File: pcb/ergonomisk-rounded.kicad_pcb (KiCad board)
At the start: 4 copper layers, 135.5 x 109 mm, 63 parts

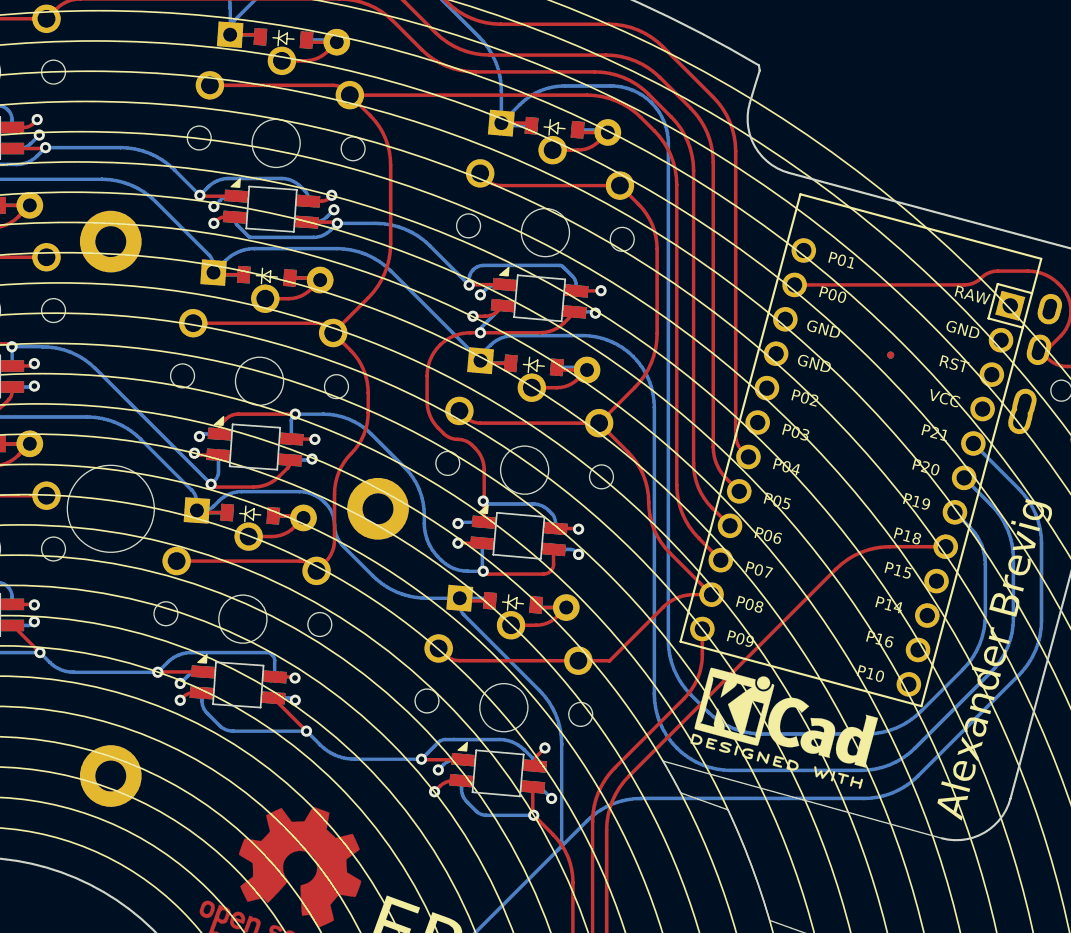
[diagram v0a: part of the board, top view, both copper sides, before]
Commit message: fix: JCL found an issue and I should've found it too
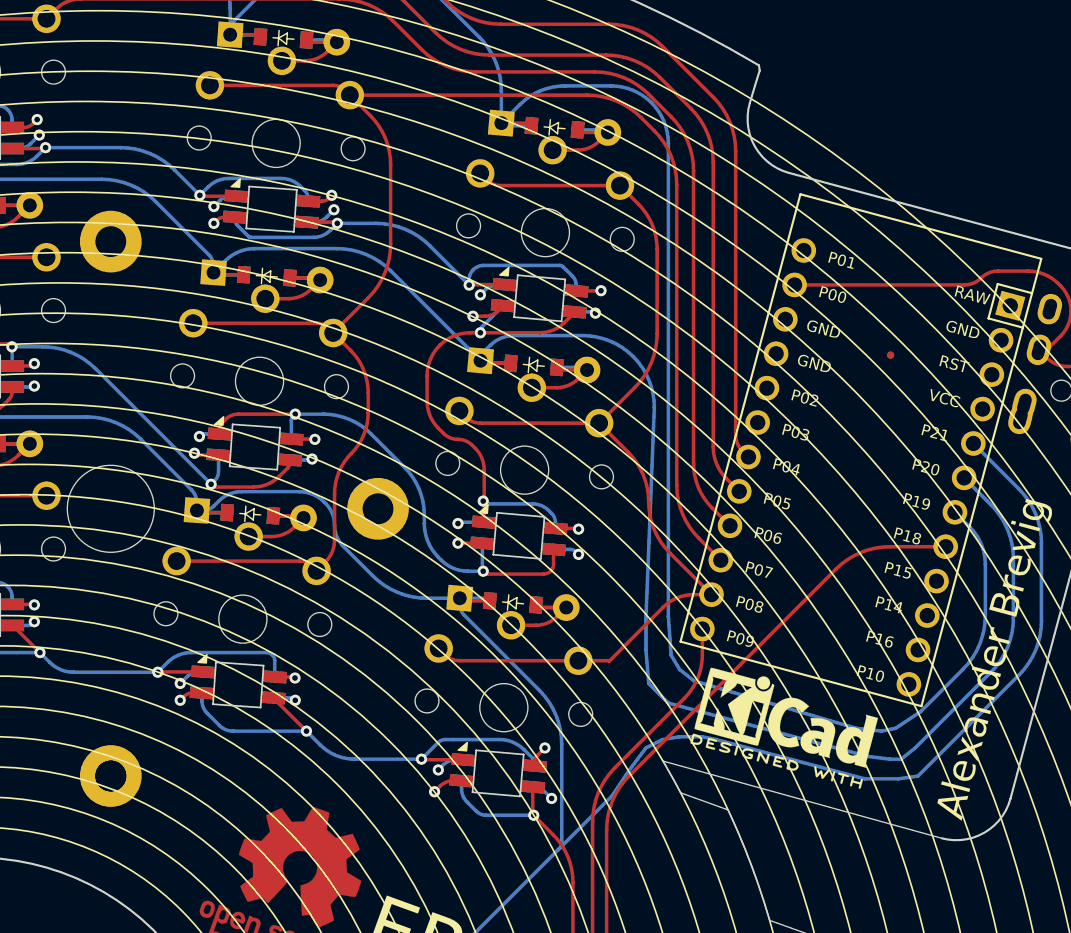
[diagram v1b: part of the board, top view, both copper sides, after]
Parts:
- added REF**: MountingHole_2.2mm_M2_DIN965_Pad_TopBottom, MountingHole:MountingHole_2.2mm_M2_DIN965_Pad_TopBottom, F.Cu at (145.1, 96.4)
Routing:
- net P20: track 198.9 -> 196.5 mm
- net P21: track 240.2 -> 242.5 mm
- net P19: track 220.0 -> 218.7 mm
